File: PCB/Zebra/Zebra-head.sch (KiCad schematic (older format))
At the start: 9 parts, among them J1 Conn_01x11, J2 MJ-4PP-9, U1 ProMicro, U2 ssd1306

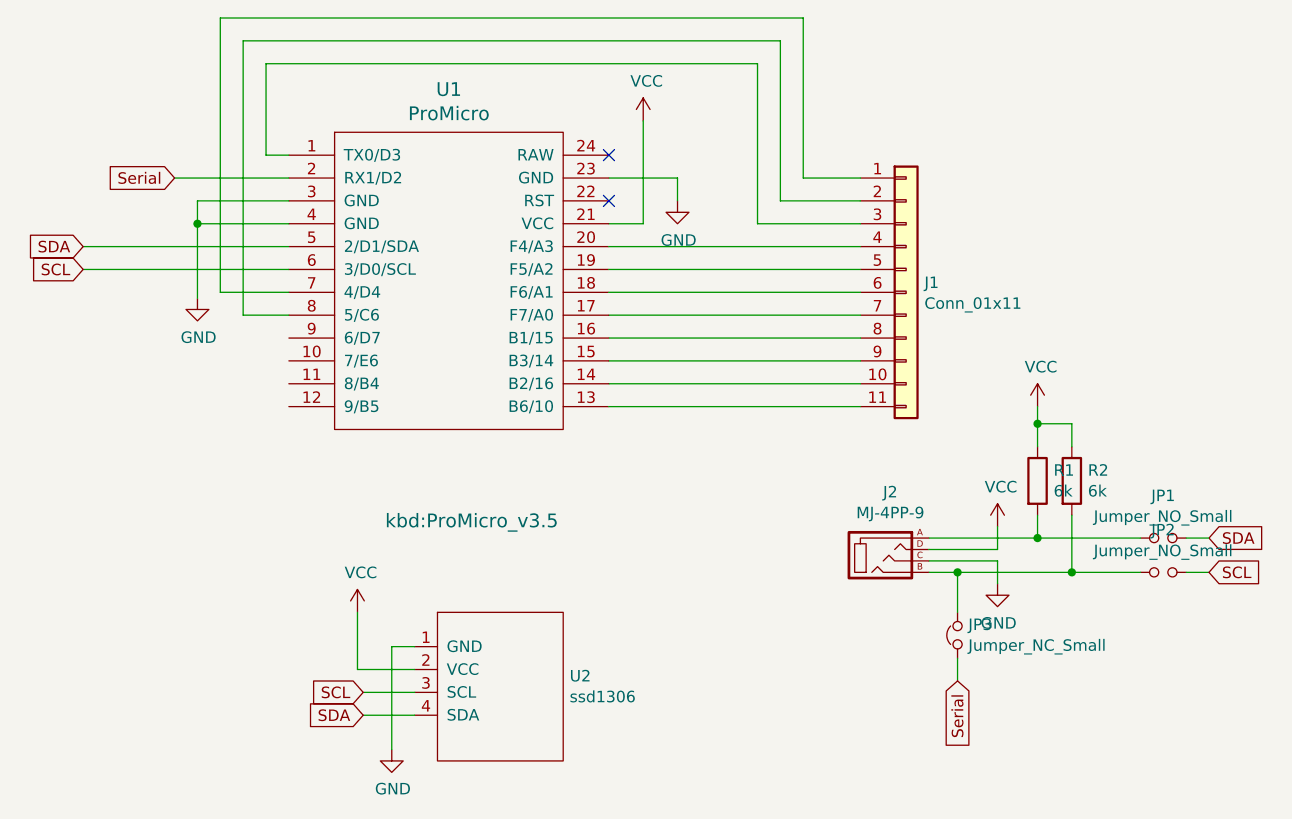
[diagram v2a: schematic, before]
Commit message: Revert "Add TRRS jack"
This reverts commit 0ecc4aa986bd018de9fb38d5a9cbe8efcda9557b.
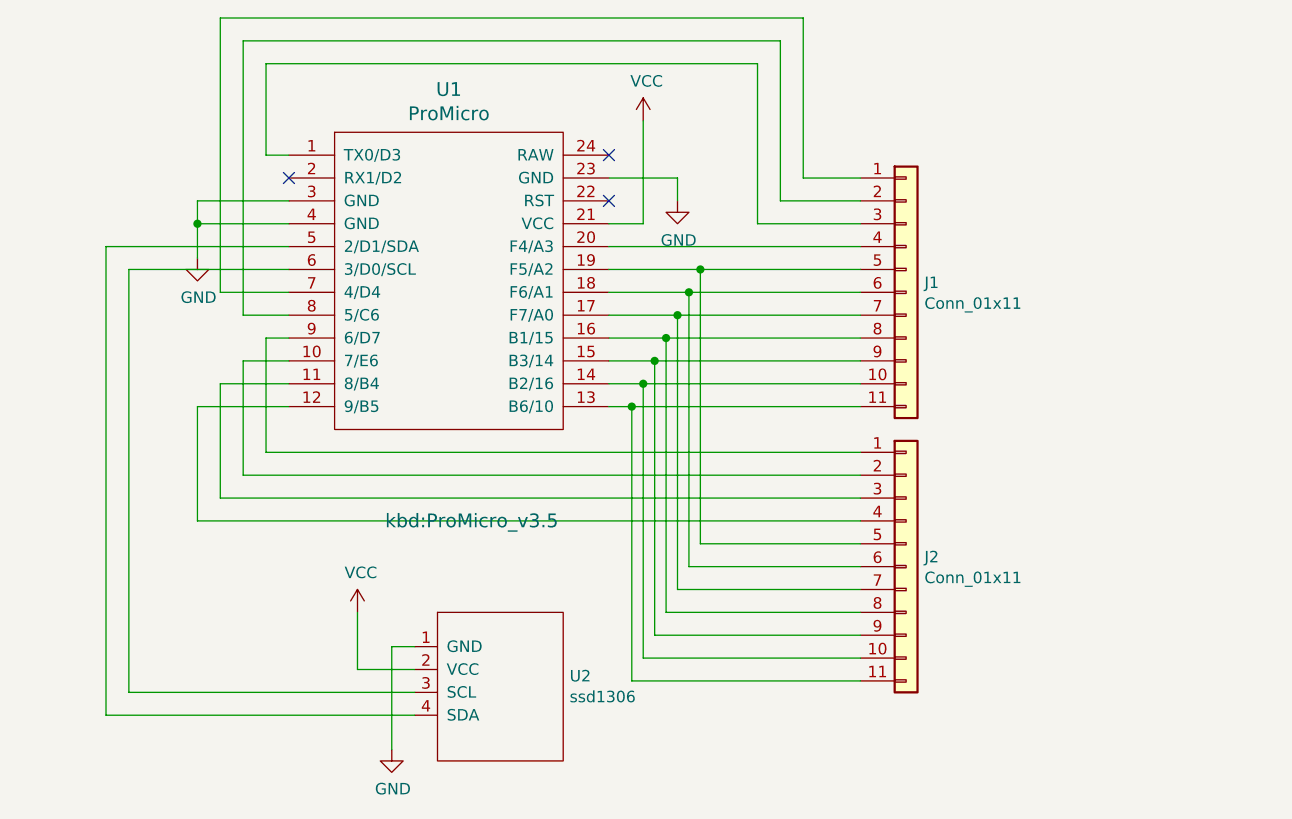
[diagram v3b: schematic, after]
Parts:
- removed J2: MJ-4PP-9, kbd:MJ-4PP-9_1side, symbol kbd:MJ-4PP-9
- removed JP1, JP2: Jumper_NO_Small, Jumper:SolderJumper-2_P1.3mm_Open_Pad1.0x1.5mm, symbol Device:Jumper_NO_Small
- removed JP3: Jumper_NC_Small, Jumper:SolderJumper-2_P1.3mm_Bridged_Pad1.0x1.5mm, symbol Device:Jumper_NC_Small
- removed R1, R2: 6k, Resistor_SMD:R_1206_3216Metric_Pad1.30x1.75mm_HandSolder, symbol Device:R
- added J2: Conn_01x11, Connector_PinHeader_2.54mm:PinHeader_1x11_P2.54mm_Vertical, symbol Connector_Generic:Conn_01x11
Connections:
- net at J1.10 (Pin_10), U1.14 (B2/16): now also J2.10 (Pin_10)
- net at J1.11 (Pin_11), U1.13 (B6/10): now also J2.11 (Pin_11)
- net at J1.5 (Pin_5), U1.19 (F5/A2): now also J2.5 (Pin_5)
- net at J1.6 (Pin_6), U1.18 (F6/A1): now also J2.6 (Pin_6)
- net at J1.7 (Pin_7), U1.17 (F7/A0): now also J2.7 (Pin_7)
- net at J1.8 (Pin_8), U1.16 (B1/15): now also J2.8 (Pin_8)
- net at J1.9 (Pin_9), U1.15 (B3/14): now also J2.9 (Pin_9)
- net at U1.10 (7/E6): now also J2.2 (Pin_2)
- net at U1.11 (8/B4): now also J2.3 (Pin_3)
- net at U1.12 (9/B5): now also J2.4 (Pin_4)
- net at U1.9 (6/D7): now also J2.1 (Pin_1)
- net SCL: no longer names the net of U1.6 (3/D0/SCL), U2.3 (SCL)
- net SDA: no longer names the net of U1.5 (2/D1/SDA), U2.4 (SDA)
- net Serial: no longer names the net of U1.2 (RX1/D2)
- no-connect marks 2 -> 3
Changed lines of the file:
@@
 	1    0    0    -1
 $EndComp
+$Comp
+L Connector_Generic:Conn_01x11 J2
+U 1 1 5FA81425
+P 4450 4300
+F 0 "J2" H 4530 4342 50  0000 L CNN
+F 1 "Conn_01x11" H 4530 4251 50  0000 L CNN
+F 2 "Connector_PinHeader_2.54mm:PinHeader_1x11_P2.54mm_Vertical" H 4450 4300 50  0001 C CNN
+F 3 "~" H 4450 4300 50  0001 C CNN
+	1    4450 4300
+	1    0    0    -1
+$EndComp
+Wire Wire Line
+	4250 3600 3250 3600
+Wire Wire Line
+	3150 3500 3300 3500
+Wire Wire Line
+	4250 3400 3350 3400
+Wire Wire Line
+	3150 3300 3400 3300
+Wire Wire Line
+	4250 3200 3450 3200
+Wire Wire Line
+	3150 3100 3500 3100
+Wire Wire Line
+	4250 3000 3550 3000
+Wire Wire Line
+	3250 3600 3250 4800
+Wire Wire Line
+	3250 4800 4250 4800
+Connection ~ 3250 3600
+Wire Wire Line
+	3250 3600 3150 3600
+Wire Wire Line
+	3300 3500 3300 4700
+Wire Wire Line
+	3300 4700 4250 4700
+Connection ~ 3300 3500
+Wire Wire Line
+	3300 3500 4250 3500
+Wire Wire Line
+	3350 3400 3350 4600
+Wire Wire Line
+	3350 4600 4250 4600
+Connection ~ 3350 3400
+Wire Wire Line
+	3350 3400 3150 3400
+Wire Wire Line
+	3400 3300 3400 4500
+Wire Wire Line
+	3400 4500 4250 4500
+Connection ~ 3400 3300
+Wire Wire Line
+	3400 3300 4250 3300
+Wire Wire Line
+	3450 3200 3450 4400
+Wire Wire Line
+	3450 4400 4250 4400
+Connection ~ 3450 3200
+Wire Wire Line
+	3450 3200 3150 3200
+Wire Wire Line
+	3500 3100 3500 4300
+Wire Wire Line
+	3500 4300 4250 4300
+Connection ~ 3500 3100
+Wire Wire Line
+	3500 3100 4250 3100
+Wire Wire Line
+	3550 3000 3550 4200
+Wire Wire Line
+	3550 4200 4250 4200
+Connection ~ 3550 3000
+Wire Wire Line
+	3550 3000 3150 3000
 Wire Wire Line
 	3150 2900 4250 2900
 Wire Wire Line
+	1650 3800 4250 3800
+Wire Wire Line
+	1550 3900 4250 3900
+Wire Wire Line
+	1450 4000 4250 4000
+Wire Wire Line
+	1350 4100 4250 4100
+Wire Wire Line
 	1750 2500 1650 2500
 Wire Wire Line
@@
 Wire Wire Line
 	1750 2800 1350 2800
+Wire Wire Line
+	1350 2800 1350 2950
 $Comp
 L power:GND #PWR01
 U 1 1 5FAB7882
-P 1350 3125
-F 0 "#PWR01" H 1350 2875 50  0001 C CNN
-F 1 "GND" H 1355 2952 50  0000 C CNN
-F 2 "" H 1350 3125 50  0001 C CNN
-F 3 "" H 1350 3125 50  0001 C CNN
-	1    1350 3125
+P 1350 2950
+F 0 "#PWR01" H 1350 2700 50  0001 C CNN
+F 1 "GND" H 1355 2777 50  0000 C CNN
+F 2 "" H 1350 2950 50  0001 C CNN
+F 3 "" H 1350 2950 50  0001 C CNN
+	1    1350 2950
 	1    0    0    -1
 $EndComp
@@
 Wire Wire Line
 	3300 2800 3300 2350
+Wire Wire Line
+	1750 3000 1050 3000
+Wire Wire Line
+	1050 4850 2300 4850
+Wire Wire Line
+	1750 2900 950  2900
+Wire Wire Line
+	950  4950 2300 4950
 $Comp
 L power:GND #PWR03
@@
 NoConn ~ 3150 2500
 NoConn ~ 3150 2700
+NoConn ~ 1750 2600
+Wire Wire Line
+	1650 3300 1750 3300
+Wire Wire Line
+	1650 3300 1650 3800
+Wire Wire Line
+	1450 3500 1750 3500
+Wire Wire Line
+	1450 3500 1450 4000
+Wire Wire Line
+	1550 3400 1750 3400
+Wire Wire Line
+	1550 3400 1550 3900
+Wire Wire Line
+	1750 3600 1350 3600
+Wire Wire Line
+	1350 3600 1350 4100
 Wire Wire Line
 	1550 3200 1750 3200
@@
 	1650 2100 3800 2100
 Wire Wire Line
-	3150 3100 4250 3100
-Wire Wire Line
-	3150 3000 4250 3000
-Wire Wire Line
-	3150 3600 4250 3600
-Wire Wire Line
-	3150 3500 4250 3500
-Wire Wire Line
-	3150 3400 4250 3400
-Wire Wire Line
-	3150 3300 4250 3300
-Wire Wire Line
-	3150 3200 4250 3200
+	1050 3000 1050 4850
+Wire Wire Line
+	950  2900 950  4950
 $Comp
 L kbd:ProMicro U1
@@
 	1    0    0    -1
 $EndComp
-Text GLabel 1250 2600 0    50   Input ~ 0
-Serial
-Wire Wire Line
-	1750 2600 1250 2600
-$Comp
-L kbd:MJ-4PP-9 J2
-U 1 1 5FD0D110
-P 4350 4250
-F 0 "J2" H 4381 4526 50  0000 C CNN
-F 1 "MJ-4PP-9" H 4381 4435 50  0000 C CNN
-F 2 "kbd:MJ-4PP-9_1side" H 4625 4425 50  0001 C CNN
-F 3 "~" H 4625 4425 50  0001 C CNN
-	1    4350 4250
-	1    0    0    -1
-$EndComp
-$Comp
-L power:VCC #PWR0101
-U 1 1 5FD0DF7B
-P 4850 4125
-F 0 "#PWR0101" H 4850 3975 50  0001 C CNN
-F 1 "VCC" H 4865 4298 50  0000 C CNN
-F 2 "" H 4850 4125 50  0001 C CNN
-F 3 "" H 4850 4125 50  0001 C CNN
-	1    4850 4125
-	1    0    0    -1
-$EndComp
-Wire Wire Line
-	4550 4225 4850 4225
-$Comp
-L power:GND #PWR0102
-U 1 1 5FD10450
-P 4850 4375
-F 0 "#PWR0102" H 4850 4125 50  0001 C CNN
-F 1 "GND" H 4855 4202 50  0000 C CNN
-F 2 "" H 4850 4375 50  0001 C CNN
-F 3 "" H 4850 4375 50  0001 C CNN
-	1    4850 4375
-	1    0    0    -1
-$EndComp
-Wire Wire Line
-	4550 4275 4850 4275
-Text GLabel 4675 4800 3    50   Input ~ 0
-Serial
-Wire Wire Line
-	4550 4325 4675 4325
-$Comp
-L Device:Jumper_NO_Small JP1
-U 1 1 5FD0D318
-P 5575 4175
-F 0 "JP1" H 5575 4360 50  0000 C CNN
-F 1 "Jumper_NO_Small" H 5575 4269 50  0000 C CNN
-F 2 "Jumper:SolderJumper-2_P1.3mm_Open_Pad1.0x1.5mm" H 5575 4175 50  0001 C CNN
-F 3 "~" H 5575 4175 50  0001 C CNN
-	1    5575 4175
-	1    0    0    -1
-$EndComp
-$Comp
-L Device:Jumper_NO_Small JP2
-U 1 1 5FD0E0A1
-P 5575 4325
-F 0 "JP2" H 5575 4510 50  0000 C CNN
-F 1 "Jumper_NO_Small" H 5575 4419 50  0000 C CNN
-F 2 "Jumper:SolderJumper-2_P1.3mm_Open_Pad1.0x1.5mm" H 5575 4325 50  0001 C CNN
-F 3 "~" H 5575 4325 50  0001 C CNN
-	1    5575 4325
-	1    0    0    -1
-$EndComp
-Wire Wire Line
-	4850 4125 4850 4225
-Wire Wire Line
-	4850 4275 4850 4375
-Text GLabel 850  2900 0    50   Input ~ 0
-SDA
-Text GLabel 850  3000 0    50   Input ~ 0
-SCL
-Wire Wire Line
-	1750 2900 850  2900
-Wire Wire Line
-	1750 3000 850  3000
-Wire Wire Line
-	1350 2800 1350 3125
-Text GLabel 2075 4950 0    50   Input ~ 0
-SDA
-Text GLabel 2075 4850 0    50   Input ~ 0
-SCL
-Wire Wire Line
-	2300 4850 2075 4850
-Wire Wire Line
-	2300 4950 2075 4950
-Text GLabel 5775 4325 2    50   Input ~ 0
-SCL
-Text GLabel 5775 4175 2    50   Input ~ 0
-SDA
-$Comp
-L power:VCC #PWR0103
-U 1 1 5FD1F947
-P 5025 3600
-F 0 "#PWR0103" H 5025 3450 50  0001 C CNN
-F 1 "VCC" H 5040 3773 50  0000 C CNN
-F 2 "" H 5025 3600 50  0001 C CNN
-F 3 "" H 5025 3600 50  0001 C CNN
-	1    5025 3600
-	1    0    0    -1
-$EndComp
-$Comp
-L Device:R R1
-U 1 1 5FD1FE92
-P 5025 3925
-F 0 "R1" H 5095 3971 50  0000 L CNN
-F 1 "6k" H 5095 3880 50  0000 L CNN
-F 2 "Resistor_SMD:R_1206_3216Metric_Pad1.30x1.75mm_HandSolder" V 4955 3925 50  0001 C CNN
-F 3 "~" H 5025 3925 50  0001 C CNN
-	1    5025 3925
-	1    0    0    -1
-$EndComp
-$Comp
-L Device:R R2
-U 1 1 5FD2335A
-P 5175 3925
-F 0 "R2" H 5245 3971 50  0000 L CNN
-F 1 "6k" H 5245 3880 50  0000 L CNN
-F 2 "Resistor_SMD:R_1206_3216Metric_Pad1.30x1.75mm_HandSolder" V 5105 3925 50  0001 C CNN
-F 3 "~" H 5175 3925 50  0001 C CNN
-	1    5175 3925
-	1    0    0    -1
-$EndComp
-Wire Wire Line
-	5025 3775 5025 3675
-Wire Wire Line
-	5175 3775 5175 3675
-Wire Wire Line
-	5175 3675 5025 3675
-Connection ~ 5025 3675
-Wire Wire Line
-	5025 3675 5025 3600
-$Comp
-L Device:Jumper_NC_Small JP3
-U 1 1 5FD2C94B
-P 4675 4600
-F 0 "JP3" V 4721 4553 50  0000 R CNN
-F 1 "Jumper_NC_Small" V 4630 4553 50  0000 R CNN
-F 2 "Jumper:SolderJumper-2_P1.3mm_Bridged_Pad1.0x1.5mm" H 4675 4600 50  0001 C CNN
-F 3 "~" H 4675 4600 50  0001 C CNN
-	1    4675 4600
-	0    -1   -1   0
-$EndComp
-Wire Wire Line
-	4675 4325 4675 4500
-Wire Wire Line
-	4675 4700 4675 4800
-Wire Wire Line
-	5675 4175 5775 4175
-Wire Wire Line
-	5675 4325 5775 4325
-Connection ~ 4675 4325
-Wire Wire Line
-	4675 4325 5175 4325
-Wire Wire Line
-	4550 4175 5025 4175
-Wire Wire Line
-	5025 4075 5025 4175
-Connection ~ 5025 4175
-Wire Wire Line
-	5025 4175 5475 4175
-Wire Wire Line
-	5175 4075 5175 4325
-Connection ~ 5175 4325
-Wire Wire Line
-	5175 4325 5475 4325
 $EndSCHEMATC
